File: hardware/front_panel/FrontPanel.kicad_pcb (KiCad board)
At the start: 4 copper layers, 198.4 x 56.2 mm, 94 parts, among them J1 FTSH-105-01-L-DV-K, J3 FFC2B35-10-T, SW2 TACT, SW6 ENCODER 24IMP, U3 VSOP38338, U4 AMS1117-3.3, U5 SSD1302Z_HALF, U7 SSD1302Z_HALF, U8 STM32F103RCTx, Y1 32.768 kHz

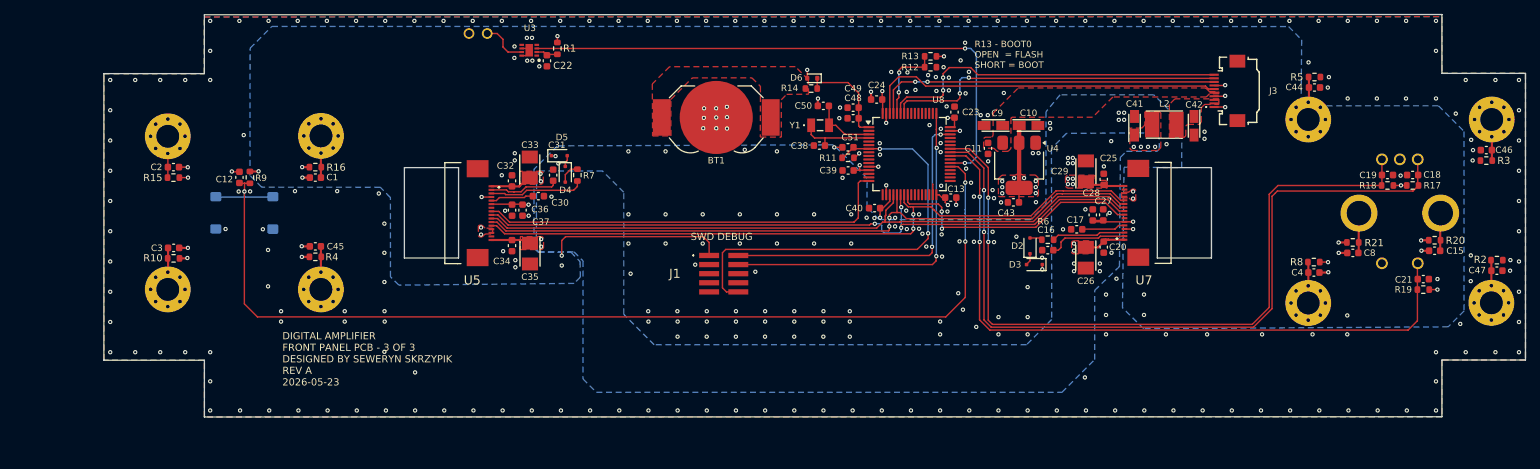
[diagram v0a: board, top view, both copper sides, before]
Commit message: swap power connectors and flip front panel PCB orientation
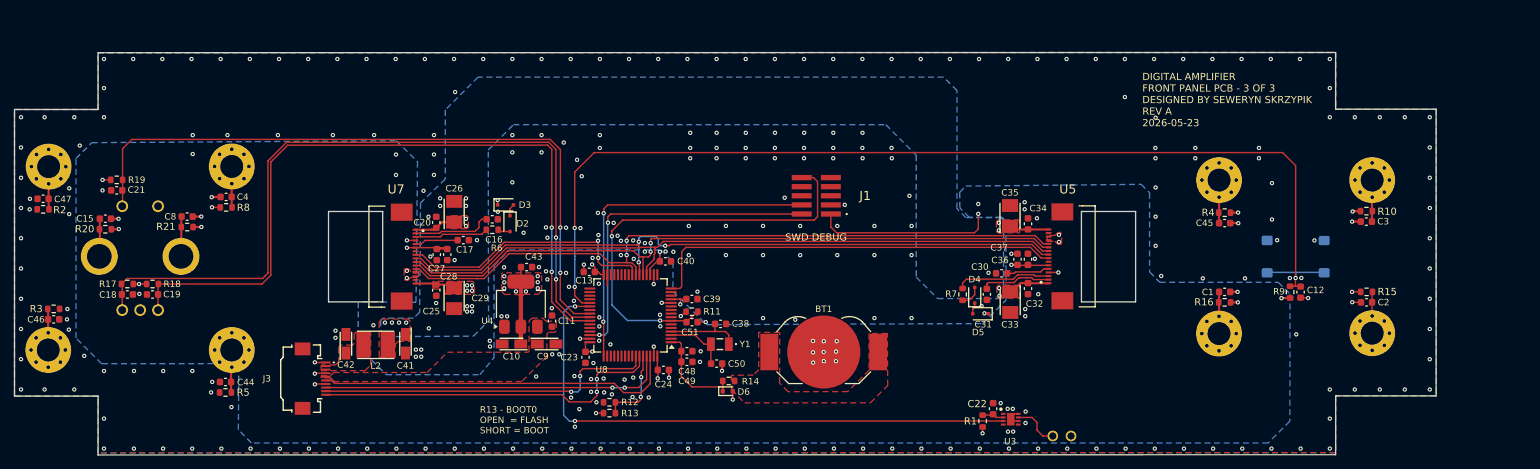
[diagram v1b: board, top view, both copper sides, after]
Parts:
- moved H7 204.0 mm to (49.8, 113.7), turned to 45 degrees
- moved C47 203.1 mm to (49.0, 92.6), turned to 180 degrees
- moved R2 203.0 mm to (49.0, 94.1), turned to 180 degrees
- moved H8 202.2 mm to (49.8, 88.1), turned to -45 degrees
- moved C46 201.3 mm to (50.5, 109.4), turned to 0 degrees
- moved R3 201.0 mm to (50.5, 108.0), turned to 0 degrees
- moved C15 185.6 mm to (57.7, 95.4), turned to 0 degrees
- moved R20 185.5 mm to (57.7, 96.8), turned to 0 degrees
- moved R19 183.0 mm to (59.3, 90.0), turned to 0 degrees
- moved C21 182.8 mm to (59.3, 91.4), turned to 180 degrees
- moved C18 180.1 mm to (60.8, 105.9), turned to 0 degrees
- moved R17 179.9 mm to (60.8, 104.5), turned to 180 degrees
- moved C19 173.2 mm to (64.3, 105.9), turned to 180 degrees
- moved R18 172.9 mm to (64.3, 104.5), turned to 0 degrees
- moved SW6 171.0 mm to (65.1, 93.6), turned to 180 degrees
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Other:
- outline, holes or cut-outs redrawn
